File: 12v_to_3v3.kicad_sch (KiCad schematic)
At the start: 6 parts, among them U4 ADP1108AR-3.3

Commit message: Woops
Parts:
- renumbered C9 to C8, C8 to C9, D1 to D2, R4 to R3, U4 to U3
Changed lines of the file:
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@@
 		(dnp no)
 		(fields_autoplaced yes)
-		(property "Reference" "#PWR014"
+		(property "Reference" "#PWR033"
 			(at 154.94 91.44 0)
 			(effects
@@
 			(project "cabinet_light"
 				(path "/8f50e6d6-3696-4153-9907-ddc1ca4e5be3/8b845be6-4642-47dd-852b-59417f6d10f3"
-					(reference "#PWR014")
+					(reference "#PWR033")
 					(unit 1)
 				)
@@
 		(on_board yes)
 		(dnp no)
-		(property "Reference" "R4"
+		(property "Reference" "R3"
 			(at 146.05 51.435 0)
 			(effects
@@
 			(project "cabinet_light"
 				(path "/8f50e6d6-3696-4153-9907-ddc1ca4e5be3/8b845be6-4642-47dd-852b-59417f6d10f3"
-					(reference "R4")
+					(reference "R3")
 					(unit 1)
 				)
@@
 		(dnp no)
 		(fields_autoplaced yes)
-		(property "Reference" "C8"
+		(property "Reference" "C9"
 			(at 176.53 80.01 0)
 			(effects
@@
 			(project "cabinet_light"
 				(path "/8f50e6d6-3696-4153-9907-ddc1ca4e5be3/8b845be6-4642-47dd-852b-59417f6d10f3"
-					(reference "C8")
+					(reference "C9")
 					(unit 1)
 				)
@@
 		(dnp no)
 		(fields_autoplaced yes)
-		(property "Reference" "D1"
+		(property "Reference" "D2"
 			(at 157.48 79.6925 90)
 			(effects
@@
 			(project "cabinet_light"
 				(path "/8f50e6d6-3696-4153-9907-ddc1ca4e5be3/8b845be6-4642-47dd-852b-59417f6d10f3"
-					(reference "D1")
+					(reference "D2")
 					(unit 1)
 				)
@@
 		(dnp no)
 		(fields_autoplaced yes)
-		(property "Reference" "#PWR013"
+		(property "Reference" "#PWR032"
 			(at 149.86 83.82 0)
 			(effects
@@
 			(project "cabinet_light"
 				(path "/8f50e6d6-3696-4153-9907-ddc1ca4e5be3/8b845be6-4642-47dd-852b-59417f6d10f3"
-					(reference "#PWR013")
+					(reference "#PWR032")
 					(unit 1)
 				)
@@
 		(on_board yes)
 		(dnp no)
-		(property "Reference" "C9"
+		(property "Reference" "C8"
 			(at 137.795 51.435 0)
 			(effects
@@
 			(project "cabinet_light"
 				(path "/8f50e6d6-3696-4153-9907-ddc1ca4e5be3/8b845be6-4642-47dd-852b-59417f6d10f3"
-					(reference "C9")
+					(reference "C8")
 					(unit 1)
 				)
@@
 		(dnp no)
 		(fields_autoplaced yes)
-		(property "Reference" "#PWR017"
+		(property "Reference" "#PWR031"
 			(at 140.97 63.5 0)
 			(effects
@@
 			(project "cabinet_light"
 				(path "/8f50e6d6-3696-4153-9907-ddc1ca4e5be3/8b845be6-4642-47dd-852b-59417f6d10f3"
-					(reference "#PWR017")
+					(reference "#PWR031")
 					(unit 1)
 				)
@@
 		(dnp no)
 		(fields_autoplaced yes)
-		(property "Reference" "#PWR015"
+		(property "Reference" "#PWR034"
 			(at 172.72 91.44 0)
 			(effects
@@
 			(project "cabinet_light"
 				(path "/8f50e6d6-3696-4153-9907-ddc1ca4e5be3/8b845be6-4642-47dd-852b-59417f6d10f3"
-					(reference "#PWR015")
+					(reference "#PWR034")
 					(unit 1)
 				)
@@
 		(dnp no)
 		(fields_autoplaced yes)
-		(property "Reference" "U4"
+		(property "Reference" "U3"
 			(at 137.795 63.6621 0)
 			(effects
@@
 			(project "cabinet_light"
 				(path "/8f50e6d6-3696-4153-9907-ddc1ca4e5be3/8b845be6-4642-47dd-852b-59417f6d10f3"
-					(reference "U4")
-					(unit 1)
-				)
+					(reference "U3")
+					(unit 1)
+				)

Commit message: Fix PCB
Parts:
- C8: footprint Capacitor_SMD:C_1206_3216Metric -> Capacitor_SMD:C_0603_1608Metric
- C9: footprint Capacitor_SMD:C_0805_2012Metric -> Capacitor_SMD:C_0603_1608Metric
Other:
- moved on the sheet: C8, C9, D2, L1, R3, U3

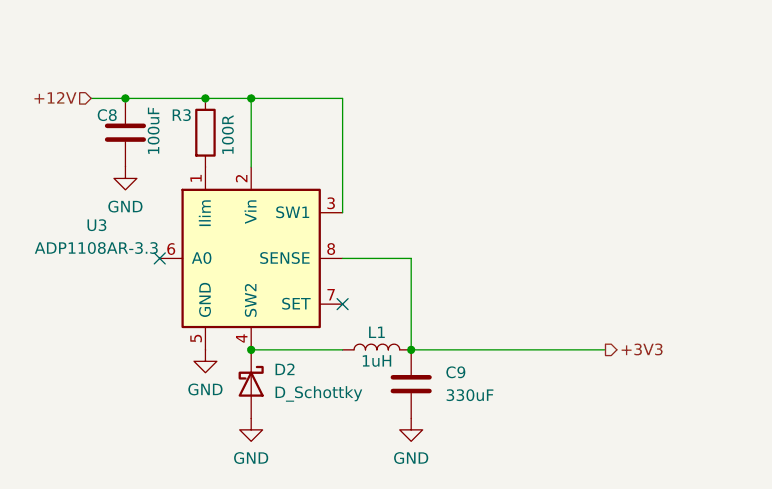
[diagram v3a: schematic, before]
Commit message: Replace power regulators; Pick all JLC components
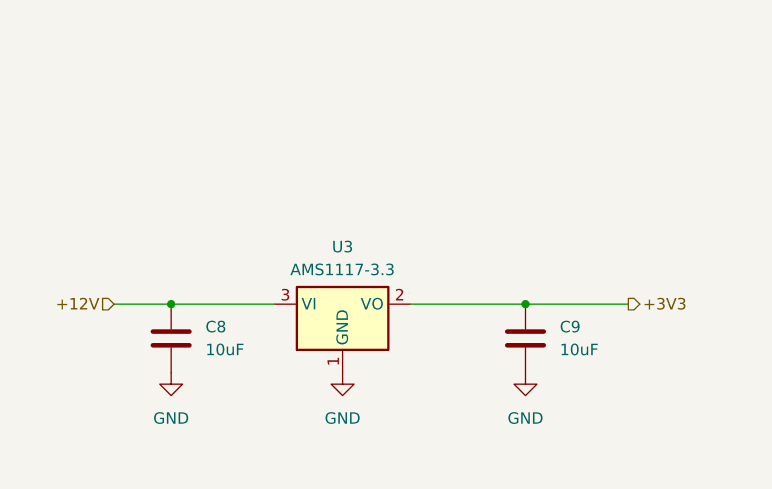
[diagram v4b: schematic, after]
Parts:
- removed D2: D_Schottky, Diode_SMD:D_0402_1005Metric, symbol Device:D_Schottky
- removed L1: 1uH, Inductor_SMD:L_0402_1005Metric, symbol Device:L
- removed R3: 100R, Resistor_SMD:R_0603_1608Metric, symbol Device:R
- removed U3: ADP1108AR-3.3, Package_SO:SOIC-8_3.9x4.9mm_P1.27mm, symbol Regulator_Switching:ADP1108AR-3.3
- added U3: AMS1117-3.3, Package_TO_SOT_SMD:SOT-223-3_TabPin2, symbol Regulator_Linear:AMS1117-3.3
- C8: value 100uF -> 10uF; footprint Capacitor_SMD:C_0603_1608Metric -> Capacitor_SMD:C_0805_2012Metric
- C9: value 330uF -> 10uF; footprint Capacitor_SMD:C_0603_1608Metric -> Capacitor_SMD:C_0805_2012Metric
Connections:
- net +12V: now also U3.3 (VI)
- net +3V3: now also U3.2 (VO)
- net GND: now also U3.1 (GND)
- no-connect marks 2 -> 0
